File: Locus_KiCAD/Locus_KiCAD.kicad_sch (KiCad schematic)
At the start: 9 parts, among them J1 LifePo4 (Vin), J2 BMS, J3 TP5000, J4 Barrel_Jack_Switch, J5 Screw_Terminal_01x04, U1 ESP32-DevKit-USB-C

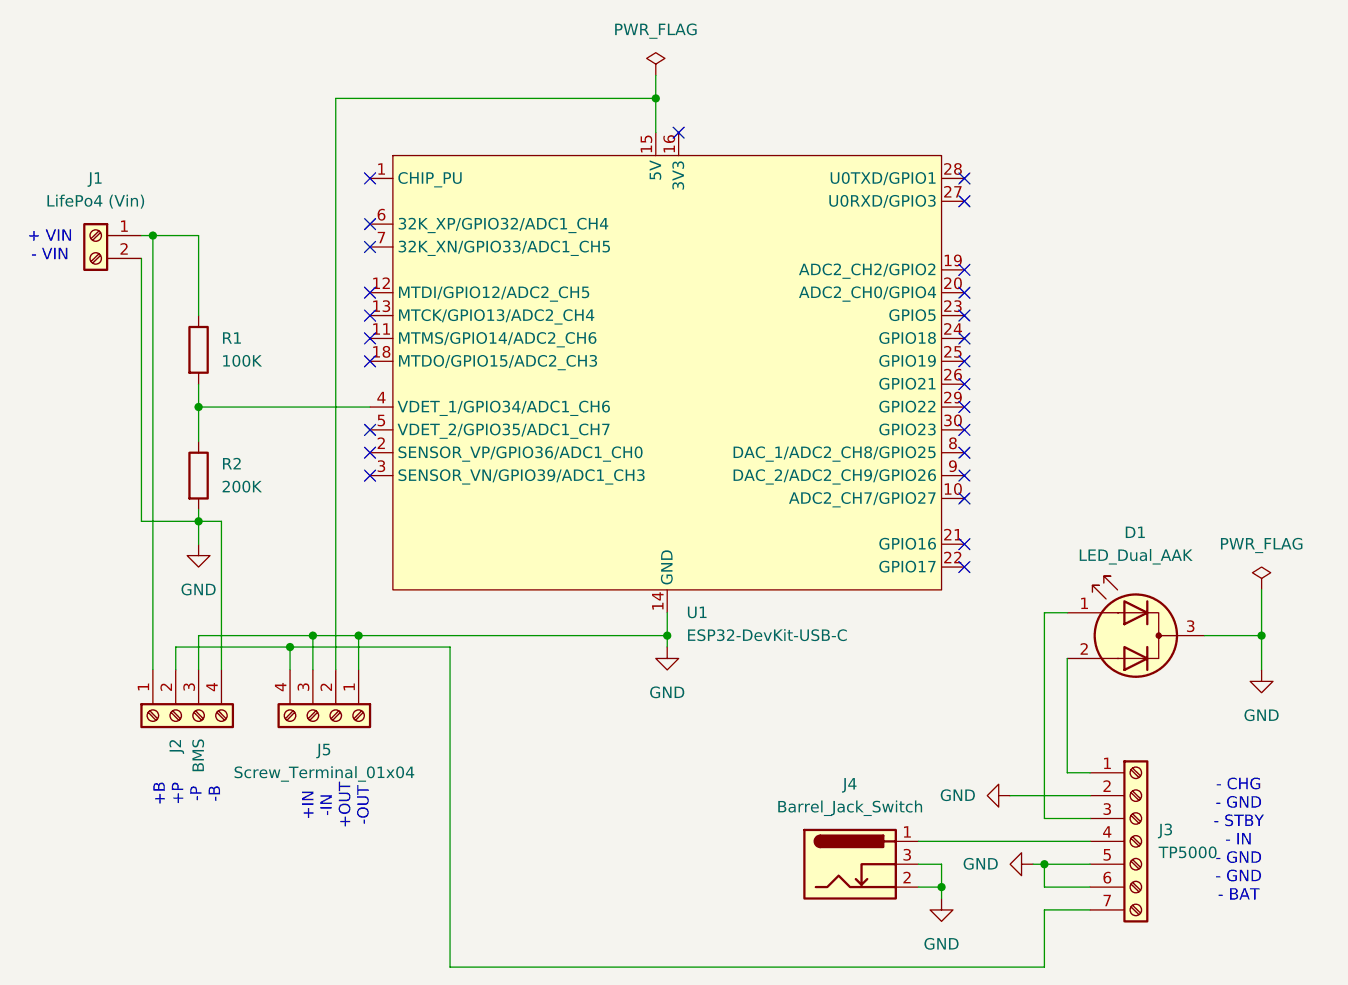
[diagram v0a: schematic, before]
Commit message: Changed schema and pcb model. Added esp 32 model
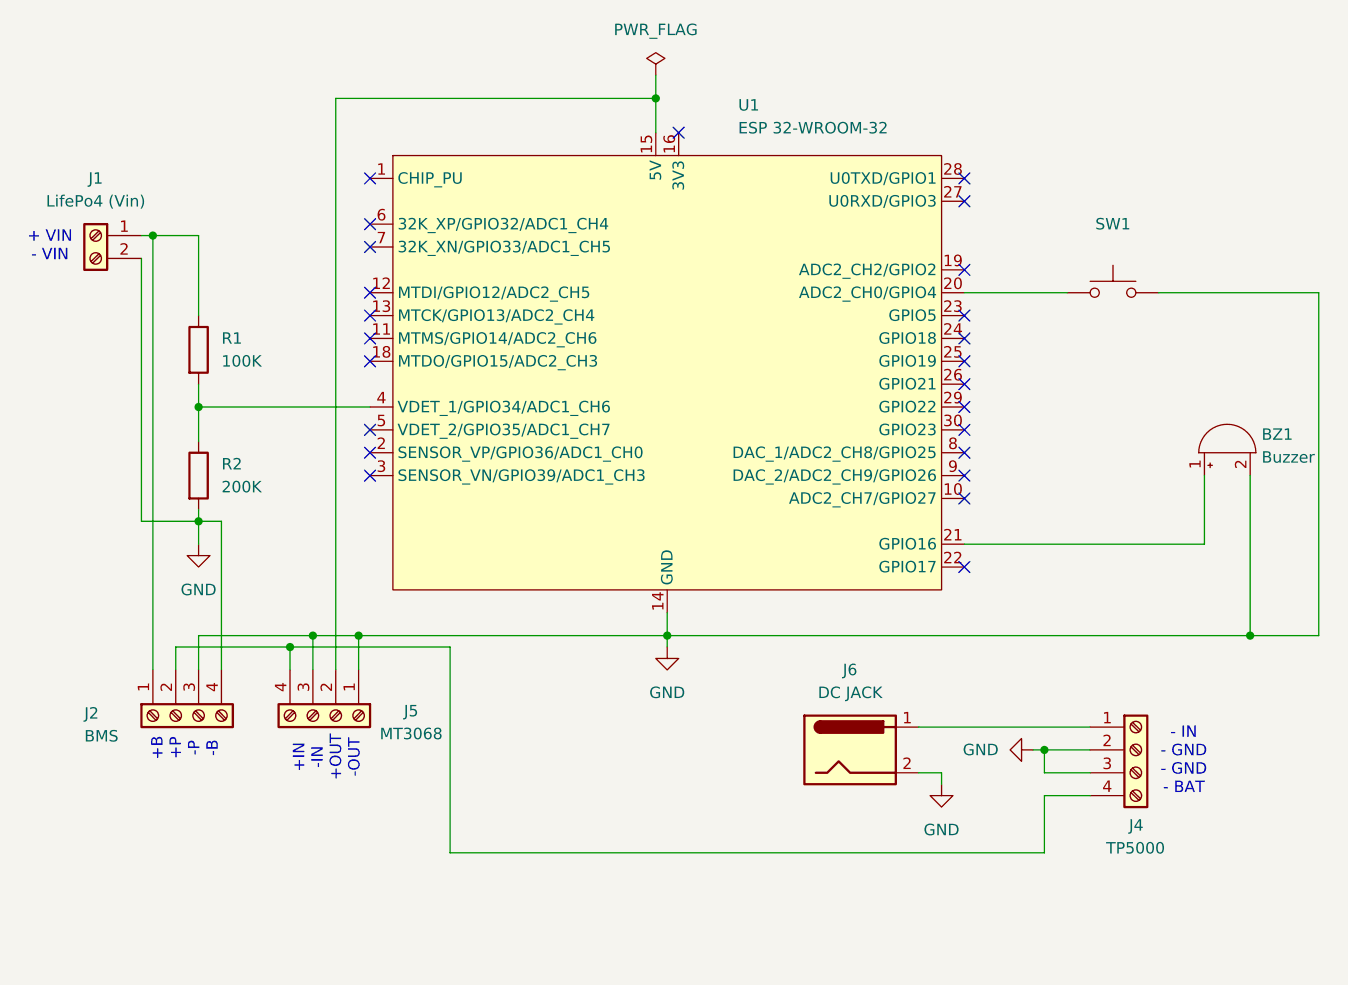
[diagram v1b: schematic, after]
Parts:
- removed D1: LED_Dual_AAK, LED_THT:LED_D3.0mm-3, symbol Device:LED_Dual_AAK
- removed J3: TP5000, TerminalBlock_Phoenix:TerminalBlock_Phoenix_MKDS-1,5-7_1x07_P5.00mm_Horizontal, symbol Connector:Screw_Terminal_01x07
- removed J4: Barrel_Jack_Switch, Connector_BarrelJack:BarrelJack_GCT_DCJ200-10-A_Horizontal, symbol Connector:Barrel_Jack_Switch
- added BZ1: Buzzer, TerminalBlock_Phoenix:TerminalBlock_Phoenix_MKDS-1,5-2_1x02_P5.00mm_Horizontal, symbol Device:Buzzer
- added J4: TP5000, TerminalBlock_Phoenix:TerminalBlock_Phoenix_MKDS-1,5-4_1x04_P5.00mm_Horizontal, symbol Connector:Screw_Terminal_01x04
- added J6: DC JACK, TerminalBlock_Phoenix:TerminalBlock_Phoenix_MKDS-1,5-2_1x02_P5.00mm_Horizontal, symbol Connector:Barrel_Jack
- added SW1: EMERGENCY BUTTON, TerminalBlock_Phoenix:TerminalBlock_Phoenix_MKDS-1,5-2_1x02_P5.00mm_Horizontal, symbol Switch:SW_Push
- J5: value Screw_Terminal_01x04 -> MT3068
- U1: value ESP32-DevKit-USB-C -> ESP 32-WROOM-32
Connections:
- net GND: now also BZ1.2 (-), J4.2 (Pin_2), J4.3 (Pin_3), J6.2, SW1.2
- net at J2.2 (Pin_2), J5.4 (Pin_4): now also J4.4 (Pin_4)
- net at U1.20 (ADC2_CH0/GPIO4): now also SW1.1
- net at U1.21 (GPIO16): now also BZ1.1 (+)
- new net: J4.1 (Pin_1), J6.1
- no-connect marks 26 -> 24
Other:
- note added: "- IN - GND - GND - BAT"
- note removed: "- CHG - GND - STBY - IN - GND - GND - BAT"

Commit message: v2.0.0 added the 3d model, closer to ending
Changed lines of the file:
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@@
+	(wire
+		(pts
+			(xy 93.98 64.77) (xy 90.17 64.77)
+		)
+		(stroke
+			(width 0)
+			(type default)
+		)
+	)
 	(wire
 		(pts
@@
 	(wire
 		(pts
-			(xy 90.17 93.98) (xy 96.52 93.98)
+			(xy 93.98 93.98) (xy 96.52 93.98)
 		)
 		(stroke
@@
 	(wire
 		(pts
-			(xy 90.17 64.77) (xy 90.17 93.98)
-		)
-		(stroke
+			(xy 93.98 64.77) (xy 93.98 93.98)
+		)
+		(stroke

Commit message: v2.1.0 added technical specs/drawings, updated the locus_cpp, updated the render.blend
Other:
- title: (none) -> Locus PCB Design
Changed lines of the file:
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@@
 	(generator_version "10.0")
 	(paper "A4")
+	(title_block
+		(title "Locus PCB Design")
+		(date "2026-10-25")
+		(rev "1 ~ M. HAQUE")
+	)
 	(text "+B\n+P\n-P\n-B"
 		(exclude_from_sim no)
